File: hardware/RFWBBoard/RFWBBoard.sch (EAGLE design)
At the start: 32 parts, among them J1 CON-71742-2184-BOT, M1 MOUNT-HOLE3.3, M2 MOUNT-HOLE3.3, M3 MOUNT-HOLE3.3, M4 MOUNT-HOLE3.3, U1 MAX2830IPC-7351, U2 LDB212G4010C-001, U3 LDB212G4010C-001, X1 LTI-SASF54GT, X2 LTI-SASF54GT

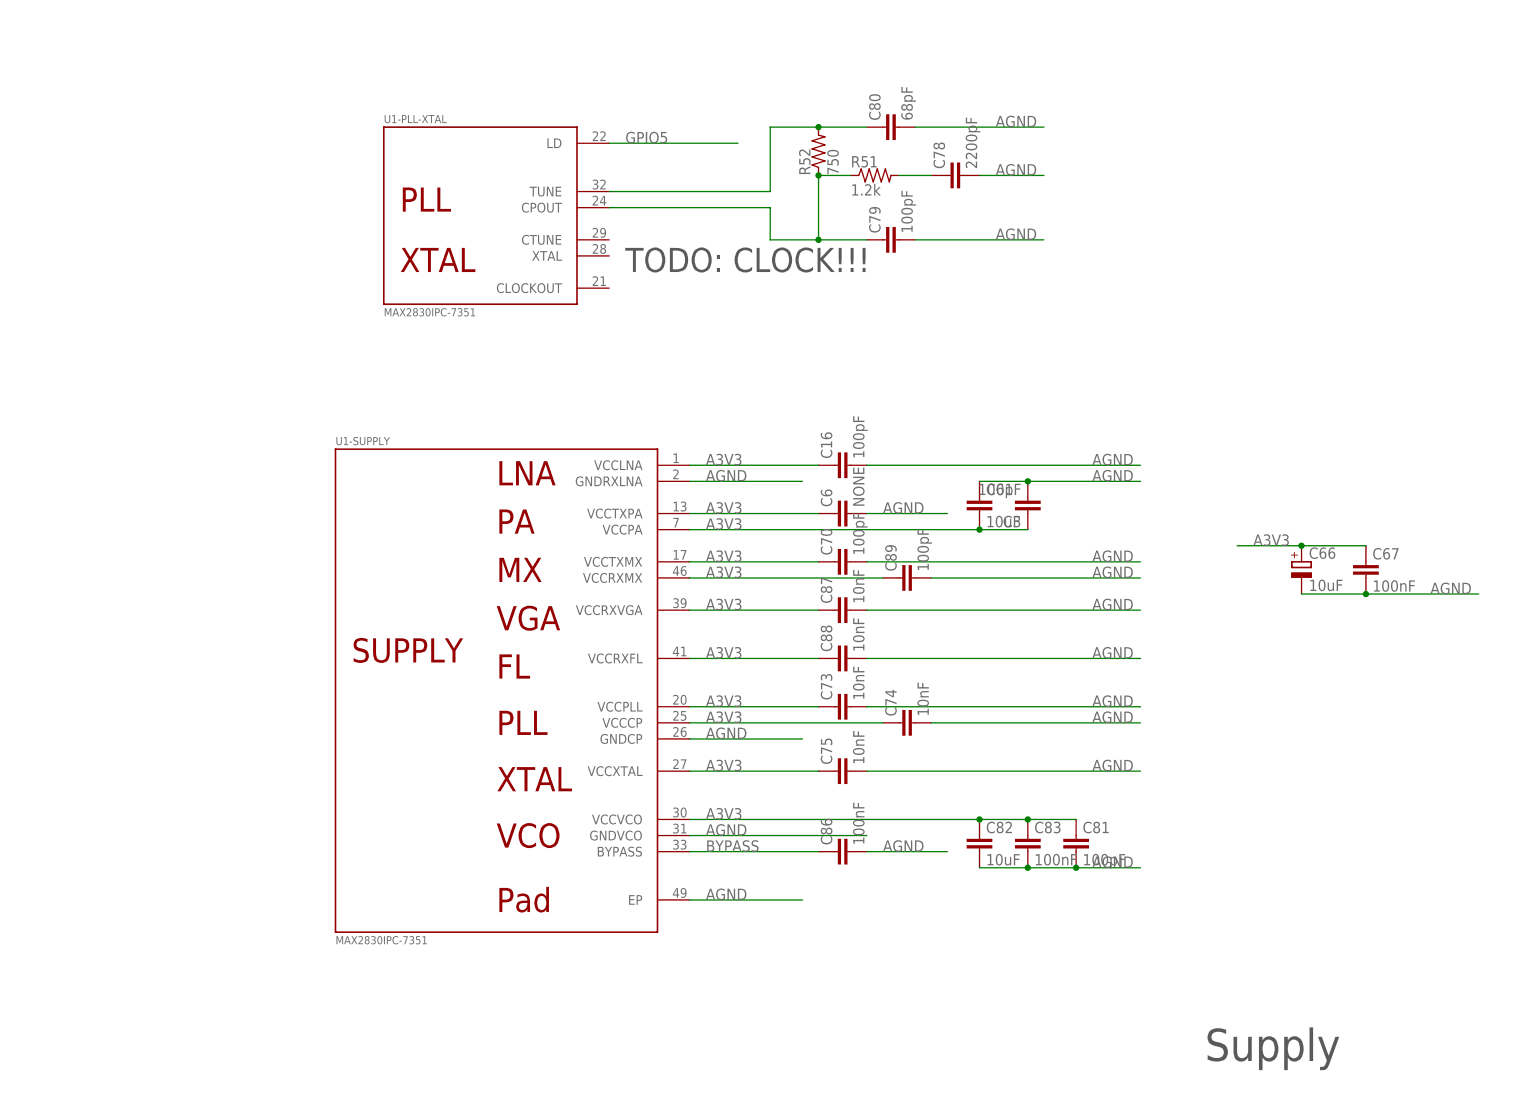
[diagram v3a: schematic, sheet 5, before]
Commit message: - Second MAX2830 - I2C EEPROM and address selector switch - GND layers
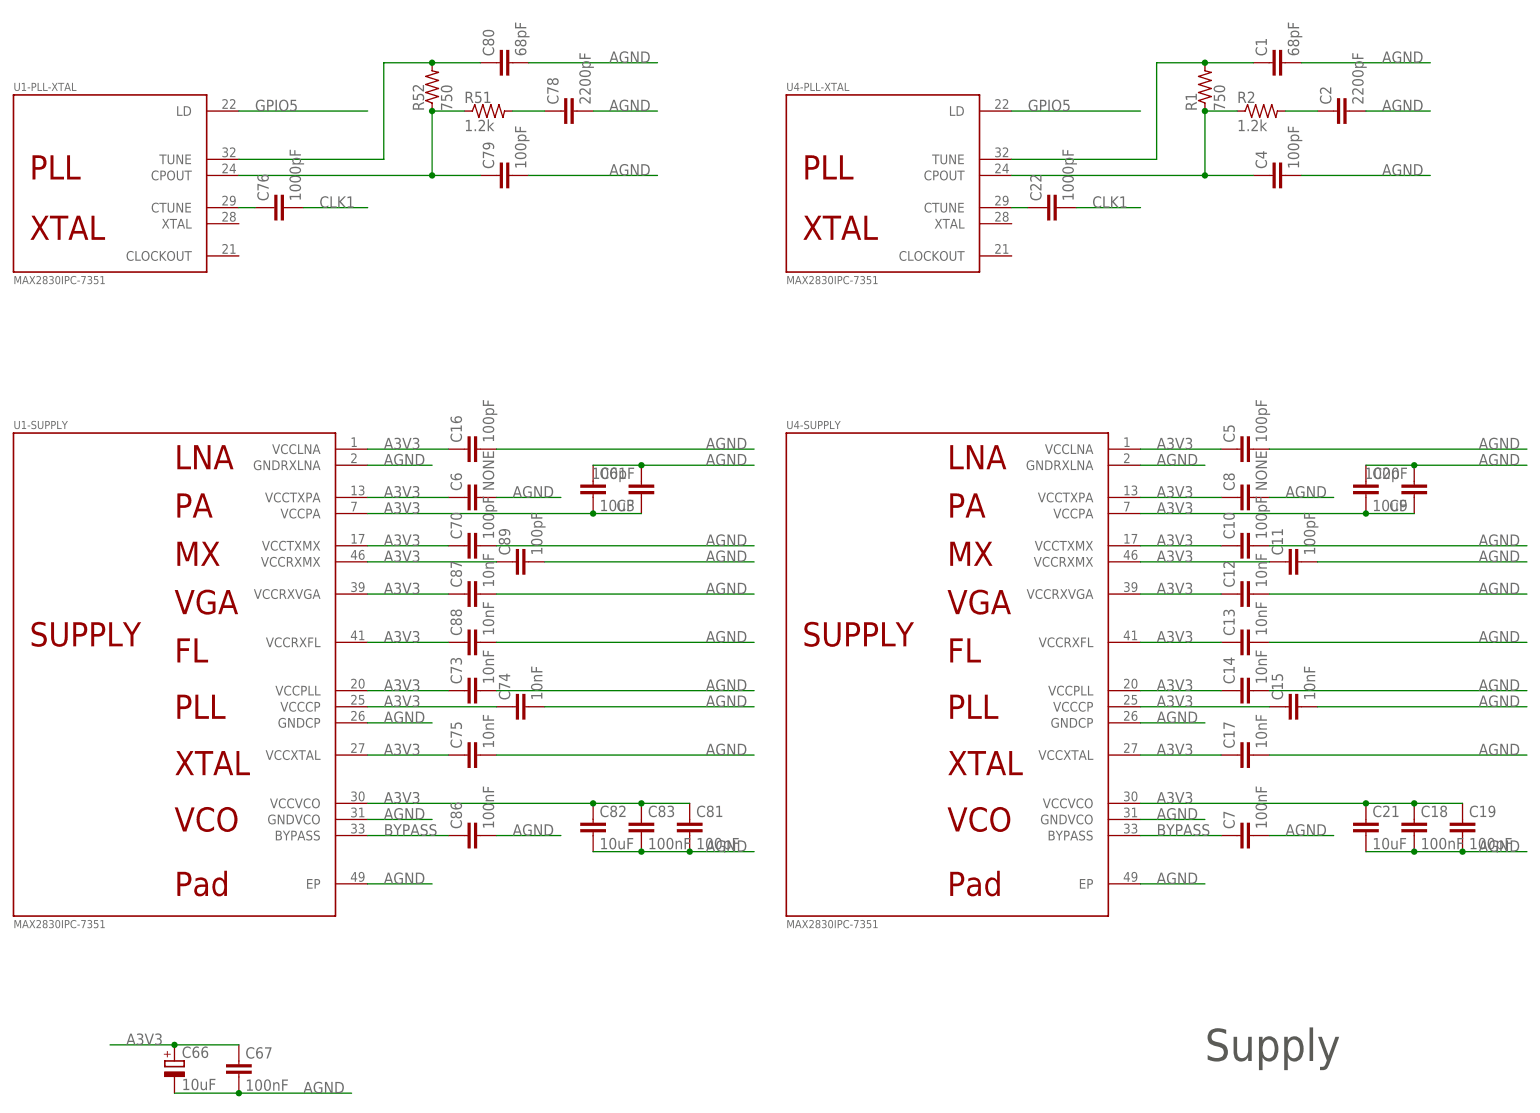
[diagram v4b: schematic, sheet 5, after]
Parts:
- added C1: 68pF, RFWBBoard:C0402
- added C10, C11, C19, C4, C5, C9: 100pF, RFWBBoard:C0402
- added C12, C13, C14, C15, C17: 10nF, RFWBBoard:C0402
- added C18, C7: 100nF, RFWBBoard:C0402
- added C2: 2200pF, RFWBBoard:C0402
- added C20: 10uF, RFWBBoard:C1206
- added C21: 10uF, RFWBBoard:C0805
- added C22, C76: 1000pF, RFWBBoard:C0402
- added C8: NONE, RFWBBoard:C0402
- added IC1: 24LC025ST, RFWBBoard:24LC025ST
- added R1: 750, RFWBBoard:R0402
- added R2: 1.2k, RFWBBoard:R0402
- added U$3: 204-214-SWITCH, RFWBBoard:204-214-SWITCH
- added U4: MAX2830IPC-7351, RFWBBoard:MAX2830IPC-7351
- added U5, U6: LDB212G4010C-001, RFWBBoard:LDB212G4010C-001
- added X3, X4: LTI-SASF54GT, RFWBBoard:LTI-SASF54GT
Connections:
- new net A0: IC1.A0, U$3.10, U$3.9
- new net A1: IC1.A1, U$3.11, U$3.12
- new net A2: IC1.A2, U$3.13, U$3.14
- new net ADCHP1: J1.55
- new net ADCHP3: J1.31
- new net CLK1: C22.2, C76.2, J1.23
- new net CLK2: J1.25
- new net N$11: C1.1, R1.2, U4-PLL-XTAL.TUNE
- new net N$12: C2.1, R2.2
- new net N$13: C4.1, R1.1, R2.1, U4-PLL-XTAL.CPOUT
- new net N$14: C22.1, U4-PLL-XTAL.CTUNE
- new net N$15: U4-ANT.ANT1+, U5.4
- new net N$16: U4-ANT.ANT2-, U6.3
- new net N$17: U4-ANT.ANT1-, U5.3
- new net N$18: U4-ANT.ANT2+, U6.4
- new net N$19: U5.1, X3G$1.1
- new net N$20: U6.1, X4G$1.1
- new net N$6: C76.1, U1-PLL-XTAL.CTUNE
- new net WP: IC1.WP, U$3.15, U$3.16
- net A3V3: now also C10.1, C11.1, C12.1, C13.1, C14.1, C15.1, C17.1, C18.1, C19.1, C20.2, C21.1, C5.1, C8.1, C9.1, U4-SUPPLY.VCCCP, U4-SUPPLY.VCCLNA, U4-SUPPLY.VCCPA, U4-SUPPLY.VCCPLL, U4-SUPPLY.VCCRXFL, U4-SUPPLY.VCCRXMX, U4-SUPPLY.VCCRXVGA, U4-SUPPLY.VCCTXMX, U4-SUPPLY.VCCTXPA, U4-SUPPLY.VCCVCO, U4-SUPPLY.VCCXTAL
- net ADC1+: now also J1.68; no longer J1.56
- net ADC1-: now also J1.66; no longer J1.54
- net ADC2+: now also J1.74; no longer J1.62
- net ADC2-: now also J1.72; no longer J1.60
- net ADC3+: now also J1.44, U4-RX.RXBBQ+; no longer J1.32
- net ADC3-: now also J1.42, U4-RX.RXBBQ-; no longer J1.30
- net ADC4+: now also J1.50, U4-RX.RXBBI+; no longer J1.38
- net ADC4-: now also J1.48, U4-RX.RXBBI-; no longer J1.36
- net ADCSF3: now also U4-CONTROL.RSSI
- net AGND: now also C1.2, C10.2, C11.2, C12.2, C13.2, C14.2, C15.2, C17.2, C18.2, C19.2, C2.2, C20.1, C21.2, C4.2, C5.2, C7.2, C8.2, C9.2, U4-SUPPLY.EP, U4-SUPPLY.GNDCP, U4-SUPPLY.GNDRXLNA, U4-SUPPLY.GNDVCO, U5.2, U5.5, U6.2, U6.5, X3G$1.GND, X3G.GND@1, X3G.GND@2, X3G.GND@3, X4G$1.GND, X4G.GND@1, X4G.GND@2, X4G.GND@3; no longer J1.31, J1.55
- net BYPASS: now also C7.1, U4-SUPPLY.BYPASS
- net D3V3: now also IC1.VCC, U$3.2, U$3.4, U$3.6, U$3.8
- net DAC1+: now also J1.56; no longer J1.68
- net DAC1-: now also J1.54; no longer J1.66
- net DAC2+: now also J1.62; no longer J1.74
- net DAC2-: now also J1.60; no longer J1.72
- net DAC3+: now also J1.32, U4-TX.TXBBQ+; no longer J1.44
- net DAC3-: now also J1.30, U4-TX.TXBBQ-; no longer J1.42
- net DAC4+: now also J1.38, U4-TX.TXBBI+; no longer J1.50
- net DAC4-: now also J1.36, U4-TX.TXBBI-; no longer J1.48
- net DACHP1: now also J1.67; no longer J1.71
- net DACHP3: now also J1.43; no longer J1.47
- net DACSF2: now also J1.71; no longer J1.67
- net DACSF4: now also J1.47; no longer J1.43
- net DGND: now also IC1.GND, U$3.1, U$3.3, U$3.5, U$3.7
- net GPIO5: now also U4-PLL-XTAL.LD
- net I2C1_SCL: now also IC1.SCL
- net I2C1_SDA: now also IC1.SDA
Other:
- note removed: "TODO: CLOCK!"
- note removed: "TODO: CLOCK!!!"
- moved on the sheet: C16, C3, C6, C61, C66, C67, C70, C73, C74, C75, C78, C79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

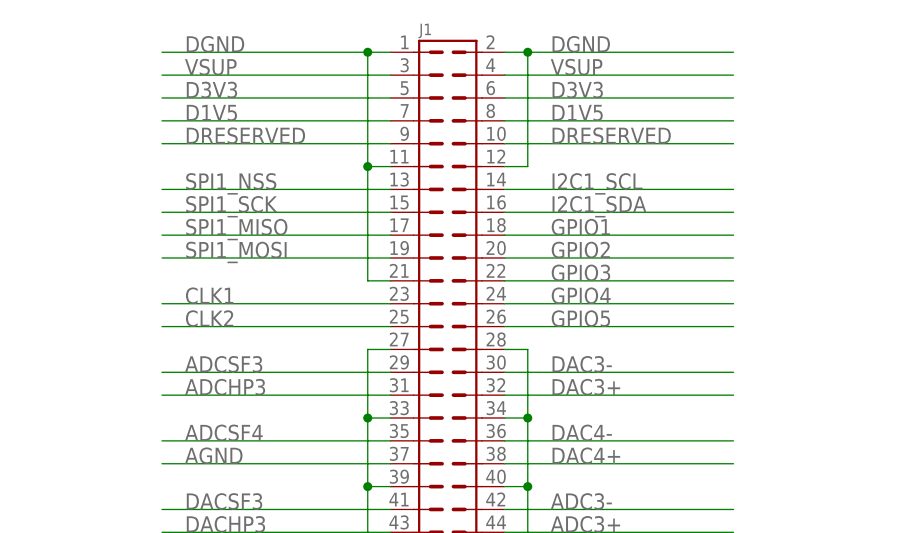
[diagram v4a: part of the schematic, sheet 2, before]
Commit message: - Started routing the MAX2830
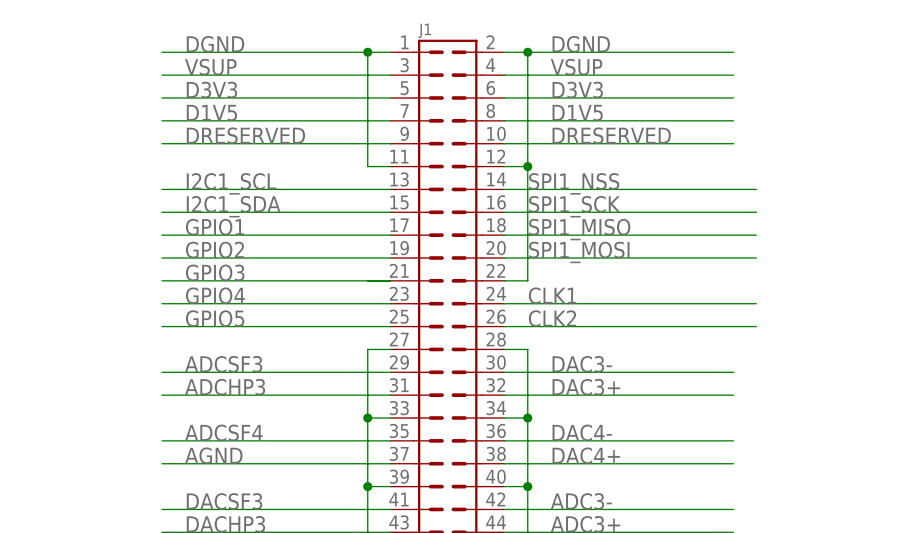
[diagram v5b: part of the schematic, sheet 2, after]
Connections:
- net CLK1: now also J1.24; no longer J1.23
- net CLK2: now also J1.26; no longer J1.25
- net DGND: now also J1.22; no longer J1.21
- net GPIO1: now also J1.17; no longer J1.18
- net GPIO2: now also J1.19; no longer J1.20
- net GPIO3: now also J1.21; no longer J1.22
- net GPIO4: now also J1.23; no longer J1.24
- net GPIO5: now also J1.25; no longer J1.26
- net I2C1_SCL: now also J1.13; no longer J1.14
- net I2C1_SDA: now also J1.15; no longer J1.16
- net SPI1_MISO: now also J1.18; no longer J1.17
- net SPI1_MOSI: now also J1.20; no longer J1.19
- net SPI1_NSS: now also J1.14; no longer J1.13
- net SPI1_SCK: now also J1.16; no longer J1.15
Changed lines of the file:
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@@
 <wire x1="127" y1="144.78" x2="127" y2="157.48" width="0.1524" layer="91"/>
 <junction x="127" y="157.48"/>
-</segment>
-<segment>
-<wire x1="111.76" y1="132.08" x2="109.22" y2="132.08" width="0.1524" layer="91"/>
-<pinref part="J1" gate="G$1" pin="21"/>
+<pinref part="J1" gate="G$1" pin="22"/>
+<wire x1="124.46" y1="132.08" x2="127" y2="132.08" width="0.1524" layer="91"/>
+<wire x1="127" y1="132.08" x2="127" y2="144.78" width="0.1524" layer="91"/>
+<junction x="127" y="144.78"/>
+</segment>
+<segment>
 <wire x1="111.76" y1="144.78" x2="109.22" y2="144.78" width="0.1524" layer="91"/>
 <pinref part="J1" gate="G$1" pin="11"/>
@@
 <wire x1="109.22" y1="157.48" x2="111.76" y2="157.48" width="0.1524" layer="91"/>
 <wire x1="109.22" y1="144.78" x2="109.22" y2="157.48" width="0.1524" layer="91"/>
-<junction x="109.22" y="144.78"/>
 <junction x="109.22" y="157.48"/>
-<wire x1="109.22" y1="132.08" x2="109.22" y2="144.78" width="0.1524" layer="91"/>
 </segment>
 </net>
@@
 <net name="SPI1_NSS" class="0">
 <segment>
-<wire x1="111.76" y1="142.24" x2="86.36" y2="142.24" width="0.1524" layer="91"/>
+<wire x1="152.4" y1="142.24" x2="124.46" y2="142.24" width="0.1524" layer="91"/>
+<label x="127" y="142.24" size="1.778" layer="95"/>
+<pinref part="J1" gate="G$1" pin="14"/>
+</segment>
+</net>
+<net name="SPI1_SCK" class="0">
+<segment>
+<wire x1="152.4" y1="139.7" x2="124.46" y2="139.7" width="0.1524" layer="91"/>
+<label x="127" y="139.7" size="1.778" layer="95"/>
+<pinref part="J1" gate="G$1" pin="16"/>
+</segment>
+</net>
+<net name="SPI1_MISO" class="0">
+<segment>
+<wire x1="124.46" y1="137.16" x2="152.4" y2="137.16" width="0.1524" layer="91"/>
+<label x="127" y="137.16" size="1.778" layer="95"/>
+<pinref part="J1" gate="G$1" pin="18"/>
+</segment>
+</net>
+<net name="SPI1_MOSI" class="0">
+<segment>
+<wire x1="124.46" y1="134.62" x2="152.4" y2="134.62" width="0.1524" layer="91"/>
+<label x="127" y="134.62" size="1.778" layer="95"/>
+<pinref part="J1" gate="G$1" pin="20"/>
+</segment>
+</net>
+<net name="I2C1_SCL" class="0">
+<segment>
+<wire x1="86.36" y1="142.24" x2="111.76" y2="142.24" width="0.1524" layer="91"/>
 <label x="88.9" y="142.24" size="1.778" layer="95"/>
 <pinref part="J1" gate="G$1" pin="13"/>
 </segment>
 </net>
-<net name="SPI1_SCK" class="0">
-<segment>
-<wire x1="111.76" y1="139.7" x2="86.36" y2="139.7" width="0.1524" layer="91"/>
+<net name="I2C1_SDA" class="0">
+<segment>
+<wire x1="86.36" y1="139.7" x2="111.76" y2="139.7" width="0.1524" layer="91"/>
 <label x="88.9" y="139.7" size="1.778" layer="95"/>
 <pinref part="J1" gate="G$1" pin="15"/>
 </segment>
 </net>
-<net name="SPI1_MISO" class="0">
-<segment>
-<wire x1="86.36" y1="137.16" x2="111.76" y2="137.16" width="0.1524" layer="91"/>
-<label x="88.9" y="137.16" size="1.778" layer="95"/>
-<pinref part="J1" gate="G$1" pin="17"/>
-</segment>
-</net>
-<net name="SPI1_MOSI" class="0">
-<segment>
-<wire x1="86.36" y1="134.62" x2="111.76" y2="134.62" width="0.1524" layer="91"/>
-<label x="88.9" y="134.62" size="1.778" layer="95"/>
-<pinref part="J1" gate="G$1" pin="19"/>
-</segment>
-</net>
-<net name="I2C1_SCL" class="0">
-<segment>
-<wire x1="124.46" y1="142.24" x2="149.86" y2="142.24" width="0.1524" layer="91"/>
-<label x="129.54" y="142.24" size="1.778" layer="95"/>
-<pinref part="J1" gate="G$1" pin="14"/>
-</segment>
-</net>
-<net name="I2C1_SDA" class="0">
-<segment>
-<wire x1="124.46" y1="139.7" x2="149.86" y2="139.7" width="0.1524" layer="91"/>
-<label x="129.54" y="139.7" size="1.778" layer="95"/>
-<pinref part="J1" gate="G$1" pin="16"/>
-</segment>
-</net>
 <net name="GPIO5" class="0">
-<segment>
-<wire x1="124.46" y1="127" x2="149.86" y2="127" width="0.1524" layer="91"/>
-<label x="129.54" y="127" size="1.778" layer="95"/>
-<pinref part="J1" gate="G$1" pin="26"/>
-</segment>
-</net>
-<net name="CLK1" class="0">
-<segment>
-<wire x1="86.36" y1="129.54" x2="111.76" y2="129.54" width="0.1524" layer="91"/>
-<label x="88.9" y="129.54" size="1.778" layer="95"/>
-<pinref part="J1" gate="G$1" pin="23"/>
-</segment>
-</net>
-<net name="CLK2" class="0">
 <segment>
 <wire x1="86.36" y1="127" x2="111.76" y2="127" width="0.1524" layer="91"/>
 <label x="88.9" y="127" size="1.778" layer="95"/>
 <pinref part="J1" gate="G$1" pin="25"/>
+</segment>
+</net>
+<net name="CLK1" class="0">
+<segment>
+<wire x1="124.46" y1="129.54" x2="152.4" y2="129.54" width="0.1524" layer="91"/>
+<label x="127" y="129.54" size="1.778" layer="95"/>
+<pinref part="J1" gate="G$1" pin="24"/>
+</segment>
+</net>
+<net name="CLK2" class="0">
+<segment>
+<wire x1="124.46" y1="127" x2="152.4" y2="127" width="0.1524" layer="91"/>
+<label x="127" y="127" size="1.778" layer="95"/>
+<pinref part="J1" gate="G$1" pin="26"/>
 </segment>
 </net>
@@
 <net name="GPIO1" class="0">
 <segment>
-<wire x1="124.46" y1="137.16" x2="149.86" y2="137.16" width="0.1524" layer="91"/>
-<label x="129.54" y="137.16" size="1.778" layer="95"/>
-<pinref part="J1" gate="G$1" pin="18"/>
+<wire x1="86.36" y1="137.16" x2="111.76" y2="137.16" width="0.1524" layer="91"/>
+<label x="88.9" y="137.16" size="1.778" layer="95"/>
+<pinref part="J1" gate="G$1" pin="17"/>
 </segment>
 </net>
 <net name="GPIO2" class="0">
 <segment>
-<wire x1="149.86" y1="134.62" x2="124.46" y2="134.62" width="0.1524" layer="91"/>
-<label x="129.54" y="134.62" size="1.778" layer="95"/>
-<pinref part="J1" gate="G$1" pin="20"/>
+<wire x1="111.76" y1="134.62" x2="86.36" y2="134.62" width="0.1524" layer="91"/>
+<label x="88.9" y="134.62" size="1.778" layer="95"/>
+<pinref part="J1" gate="G$1" pin="19"/>
 </segment>
 </net>
 <net name="GPIO3" class="0">
 <segment>
-<wire x1="124.46" y1="132.08" x2="149.86" y2="132.08" width="0.1524" layer="91"/>
-<label x="129.54" y="132.08" size="1.778" layer="95"/>
-<pinref part="J1" gate="G$1" pin="22"/>
+<wire x1="86.36" y1="132.08" x2="111.76" y2="132.08" width="0.1524" layer="91"/>
+<label x="88.9" y="132.08" size="1.778" layer="95"/>
+<pinref part="J1" gate="G$1" pin="21"/>
+<wire x1="111.76" y1="132.08" x2="109.22" y2="132.08" width="0.1524" layer="91"/>
 </segment>
 </net>
 <net name="GPIO4" class="0">
 <segment>
-<wire x1="124.46" y1="129.54" x2="149.86" y2="129.54" width="0.1524" layer="91"/>
-<label x="129.54" y="129.54" size="1.778" layer="95"/>
-<pinref part="J1" gate="G$1" pin="24"/>
-</segment>
-</net>
+<wire x1="86.36" y1="129.54" x2="111.76" y2="129.54" width="0.1524" layer="91"/>
+<label x="88.9" y="129.54" size="1.778" layer="95"/>
+<pinref part="J1" gate="G$1" pin="23"/>
+</segment>
+</net>
